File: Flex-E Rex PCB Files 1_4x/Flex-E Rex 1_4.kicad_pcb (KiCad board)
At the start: 2 copper layers, 52.2 x 33.4 mm, 7 parts, among them J1 Conn_01x02_Pin, SW1 1825232-1

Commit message: Changed PCB version ID to X.X.X format
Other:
- board text added: "1.4x 2.2.X"
- board text removed: "1.4x V0.2"

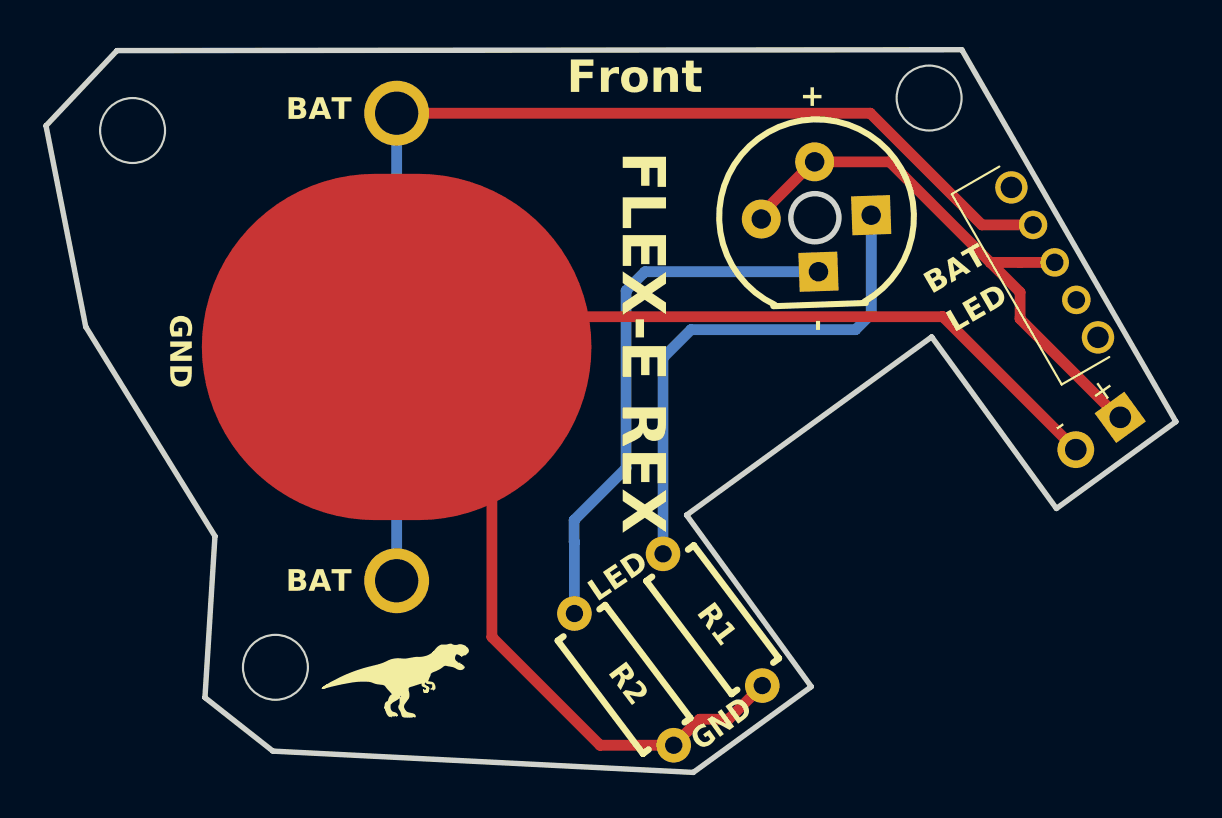
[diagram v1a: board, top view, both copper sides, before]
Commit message: added new PCB version. Increased size of pads and flipped the solder pad side for the LEDs
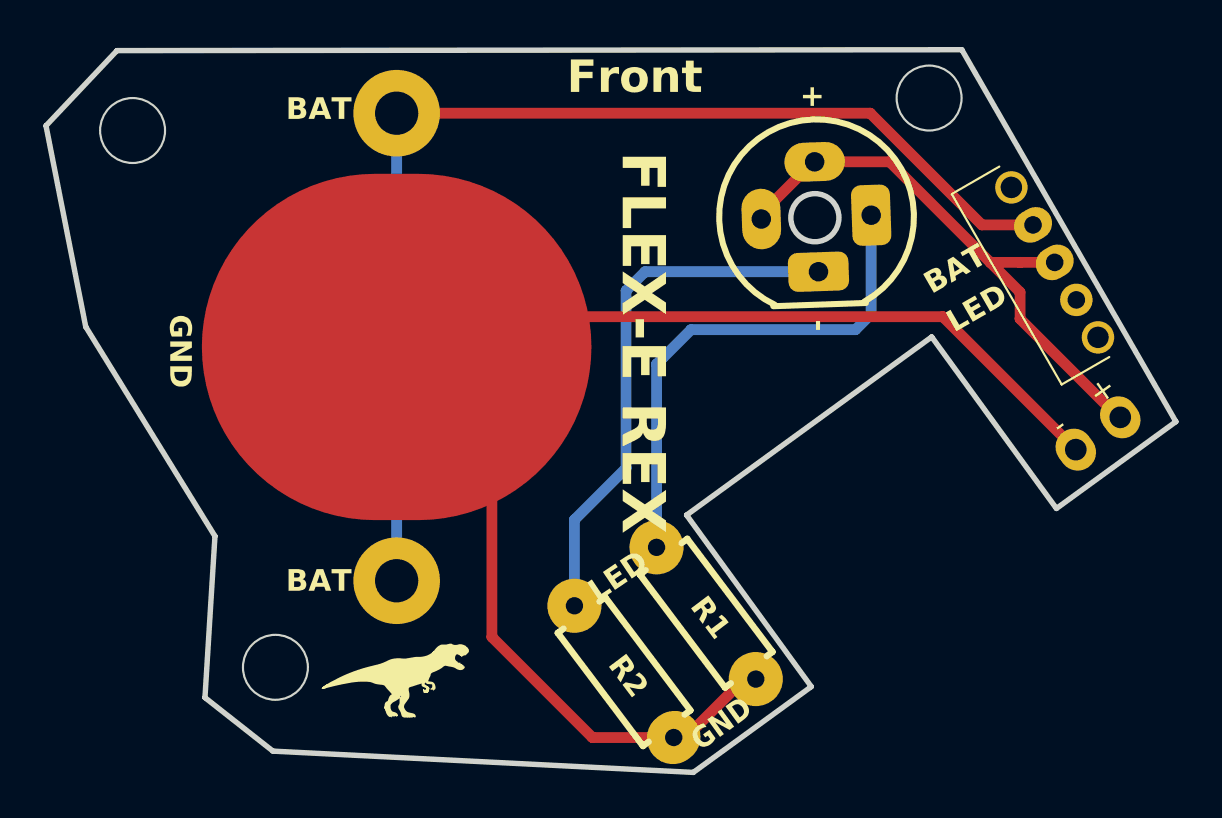
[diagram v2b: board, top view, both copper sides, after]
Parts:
- moved R1 0.42 mm to (73.8, 54.7)
- moved R2 0.36 mm to (70.0, 57.4)
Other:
- board text added: "1.4x 2.3.X"
- board text removed: "1.4x 2.2.X"
